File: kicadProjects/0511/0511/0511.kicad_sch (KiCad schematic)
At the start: 28 parts, among them U1 UDA1334A_Breakout, U2 YAAJ_BlackPill, U3 MCP23017, U4 MCP23017, U5 MCP23017, U6 MCP23017, U7 CP2102N-Axx-xQFN24, U8 STM32F411RETx

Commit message: updated backups
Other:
- added sheet Untitled Sheet (untitled.kicad_sch)
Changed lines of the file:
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@@
+	)
+	(sheet
+		(at 260.35 245.11)
+		(size 12.7 3.81)
+		(exclude_from_sim no)
+		(in_bom yes)
+		(on_board yes)
+		(dnp no)
+		(fields_autoplaced yes)
+		(stroke
+			(width 0.1524)
+			(type solid)
+		)
+		(fill
+			(color 0 0 0 0.0000)
+		)
+		(property "Sheetname" "Untitled Sheet"
+			(at 260.35 244.3984 0)
+			(effects
+				(font
+					(size 1.27 1.27)
+				)
+				(justify left bottom)
+			)
+		)
+		(property "Sheetfile" "untitled.kicad_sch"
+			(at 260.35 249.5046 0)
+			(effects
+				(font
+					(size 1.27 1.27)
+				)
+				(justify left top)
+			)
+		)
+		(pin "test" input
+			(at 260.35 247.65 180)
+			(effects
+				(font
+					(size 1.27 1.27)
+				)
+				(justify left)
+			)
+		)
+		(instances
+			(project "0511"
+				(path "/2c0b0e0d-c5e7-48b7-93bb-9be1941509af"
+					(page "69")
+				)
+			)
+		)
 	)
 	(sheet

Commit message: started alim bloc
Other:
- removed sheet Untitled Sheet
- added sheet Buck (buck.kicad_sch)
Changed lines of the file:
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@@
 	(wire
 		(pts
+			(xy 303.53 229.87) (xy 303.53 234.95)
+		)
+		(stroke
+			(width 0)
+			(type default)
+		)
+	)
+	(wire
+		(pts
 			(xy 320.04 50.8) (xy 320.04 53.34)
 		)
@@
 	(wire
 		(pts
+			(xy 266.7 234.95) (xy 266.7 240.03)
+		)
+		(stroke
+			(width 0)
+			(type default)
+		)
+	)
+	(wire
+		(pts
 			(xy 228.6 63.5) (xy 228.6 69.85)
 		)
@@
 	(wire
 		(pts
+			(xy 262.89 240.03) (xy 266.7 240.03)
+		)
+		(stroke
+			(width 0)
+			(type default)
+		)
+	)
+	(wire
+		(pts
 			(xy 156.21 165.1) (xy 156.21 143.51)
 		)
@@
 	(wire
 		(pts
+			(xy 303.53 234.95) (xy 285.75 234.95)
+		)
+		(stroke
+			(width 0)
+			(type default)
+		)
+	)
+	(wire
+		(pts
+			(xy 273.05 234.95) (xy 266.7 234.95)
+		)
+		(stroke
+			(width 0)
+			(type default)
+		)
+	)
+	(wire
+		(pts
 			(xy 331.47 36.83) (xy 331.47 43.18)
 		)
@@
 	)
 	(symbol
+		(lib_id "power:+3.3V")
+		(at 303.53 229.87 0)
+		(unit 1)
+		(exclude_from_sim no)
+		(in_bom yes)
+		(on_board yes)
+		(dnp no)
+		(fields_autoplaced yes)
+		(property "Reference" "#PWR044"
+			(at 303.53 233.68 0)
+			(effects
+				(font
+					(size 1.27 1.27)
+				)
+				(hide yes)
+			)
+		)
+		(property "Value" "+3.3V"
+			(at 303.53 224.79 0)
+			(effects
+				(font
+					(size 1.27 1.27)
+				)
+			)
+		)
+		(property "Footprint" ""
+			(at 303.53 229.87 0)
+			(effects
+				(font
+					(size 1.27 1.27)
+				)
+				(hide yes)
+			)
+		)
+		(property "Datasheet" ""
+			(at 303.53 229.87 0)
+			(effects
+				(font
+					(size 1.27 1.27)
+				)
+				(hide yes)
+			)
+		)
+		(property "Description" "Power symbol creates a global label with name \"+3.3V\""
+			(at 303.53 229.87 0)
+			(effects
+				(font
+					(size 1.27 1.27)
+				)
+				(hide yes)
+			)
+		)
+		(pin "1"
+		)
+		(instances
+			(project "0511"
+				(path "/2c0b0e0d-c5e7-48b7-93bb-9be1941509af"
+					(reference "#PWR044")
+					(unit 1)
+				)
+			)
+		)
+	)
+	(symbol
 		(lib_id "Device:C")
 		(at 34.29 109.22 0)
@@
 	)
 	(symbol
+		(lib_id "power:GND")
+		(at 262.89 240.03 0)
+		(unit 1)
+		(exclude_from_sim no)
+		(in_bom yes)
+		(on_board yes)
+		(dnp no)
+		(fields_autoplaced yes)
+		(property "Reference" "#PWR045"
+			(at 262.89 246.38 0)
+			(effects
+				(font
+					(size 1.27 1.27)
+				)
+				(hide yes)
+			)
+		)
+		(property "Value" "GND"
+			(at 262.89 245.11 0)
+			(effects
+				(font
+					(size 1.27 1.27)
+				)
+			)
+		)
+		(property "Footprint" ""
+			(at 262.89 240.03 0)
+			(effects
+				(font
+					(size 1.27 1.27)
+				)
+				(hide yes)
+			)
+		)
+		(property "Datasheet" ""
+			(at 262.89 240.03 0)
+			(effects
+				(font
+					(size 1.27 1.27)
+				)
+				(hide yes)
+			)
+		)
+		(property "Description" "Power symbol creates a global label with name \"GND\" , ground"
+			(at 262.89 240.03 0)
+			(effects
+				(font
+					(size 1.27 1.27)
+				)
+				(hide yes)
+			)
+		)
+		(pin "1"
+		)
+		(instances
+			(project "0511"
+				(path "/2c0b0e0d-c5e7-48b7-93bb-9be1941509af"
+					(reference "#PWR045")
+					(unit 1)
+				)
+			)
+		)
+	)
+	(symbol
 		(lib_id "power:+3.3V")
 		(at 67.31 86.36 0)
@@
 	)
 	(sheet
+		(at 273.05 232.41)
+		(size 12.7 3.81)
+		(exclude_from_sim no)
+		(in_bom yes)
+		(on_board yes)
+		(dnp no)
+		(fields_autoplaced yes)
+		(stroke
+			(width 0.1524)
+			(type solid)
+		)
+		(fill
+			(color 0 0 0 0.0000)
+		)
+		(property "Sheetname" "Buck"
+			(at 273.05 231.6984 0)
+			(effects
+				(font
+					(size 1.27 1.27)
+				)
+				(justify left bottom)
+			)
+		)
+		(property "Sheetfile" "buck.kicad_sch"
+			(at 273.05 236.8046 0)
+			(effects
+				(font
+					(size 1.27 1.27)
+				)
+				(justify left top)
+			)
+		)
+		(pin "3.3v" input
+			(at 285.75 234.95 0)
+			(effects
+				(font
+					(size 1.27 1.27)
+				)
+				(justify right)
+			)
+		)
+		(pin "gnd" passive
+			(at 273.05 234.95 180)
+			(effects
+				(font
+					(size 1.27 1.27)
+				)
+				(justify left)
+			)
+		)
+		(instances
+			(project "0511"
+				(path "/2c0b0e0d-c5e7-48b7-93bb-9be1941509af"
+					(page "69")
+				)
+			)
+		)
+	)
+	(sheet
 		(at 147.32 167.64)
 		(size 12.7 3.81)
@@
 				)
 			)
-		)
-	)
-	(sheet
-		(at 260.35 245.11)
-		(size 12.7 3.81)
-		(exclude_from_sim no)
-		(in_bom yes)
-		(on_board yes)
-		(dnp no)
-		(fields_autoplaced yes)
-		(stroke
-			(width 0.1524)
-			(type solid)
-		)
-		(fill
-			(color 0 0 0 0.0000)
-		)
-		(property "Sheetname" "Untitled Sheet"
-			(at 260.35 244.3984 0)
-			(effects
-				(font
-					(size 1.27 1.27)
-				)
-				(justify left bottom)
-			)
-		)
-		(property "Sheetfile" "untitled.kicad_sch"
-			(at 260.35 249.5046 0)
-			(effects
-				(font
-					(size 1.27 1.27)
-				)
-				(justify left top)
-			)
-		)
-		(pin "test" input
-			(at 260.35 247.65 180)
-			(effects
-				(font
-					(size 1.27 1.27)
-				)
-				(justify left)
-			)
-		)
-		(instances
-			(project "0511"
-				(path "/2c0b0e0d-c5e7-48b7-93bb-9be1941509af"
-					(page "69")
-				)
-			)

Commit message: started stm32 hierarchical b=view scheme
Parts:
- removed U8: STM32F411RETx, Package_QFP:LQFP-64_10x10mm_P0.5mm, symbol MCU_ST_STM32F4:STM32F411RETx
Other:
- added sheet Stm32f411retx (stm32f411retx.kicad_sch)
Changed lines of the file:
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@@
 	)
 	(symbol
-		(lib_id "MCU_ST_STM32F4:STM32F411RETx")
-		(at 88.9 251.46 90)
-		(unit 1)
-		(exclude_from_sim no)
-		(in_bom yes)
-		(on_board yes)
-		(dnp no)
-		(fields_autoplaced yes)
-		(property "Reference" "U8"
-			(at 140.97 243.4746 90)
-			(effects
-				(font
-					(size 1.27 1.27)
-				)
-			)
-		)
-		(property "Value" "STM32F411RETx"
-			(at 140.97 246.0146 90)
-			(effects
-				(font
-					(size 1.27 1.27)
-				)
-			)
-		)
-		(property "Footprint" "Package_QFP:LQFP-64_10x10mm_P0.5mm"
-			(at 132.08 266.7 0)
-			(effects
-				(font
-					(size 1.27 1.27)
-				)
-				(justify right)
-				(hide yes)
-			)
-		)
-		(property "Datasheet" "https://www.st.com/resource/en/datasheet/stm32f411re.pdf"
-			(at 88.9 251.46 0)
-			(effects
-				(font
-					(size 1.27 1.27)
-				)
-				(hide yes)
-			)
-		)
-		(property "Description" "STMicroelectronics Arm Cortex-M4 MCU, 512KB flash, 128KB RAM, 100 MHz, 1.7-3.6V, 50 GPIO, LQFP64"
-			(at 88.9 251.46 0)
-			(effects
-				(font
-					(size 1.27 1.27)
-				)
-				(hide yes)
-			)
-		)
-		(pin "17"
-		)
-		(pin "52"
-		)
-		(pin "40"
-		)
-		(pin "27"
-		)
-		(pin "59"
-		)
-		(pin "23"
-		)
-		(pin "60"
-		)
-		(pin "54"
-		)
-		(pin "36"
-		)
-		(pin "2"
-		)
-		(pin "26"
-		)
-		(pin "37"
-		)
-		(pin "9"
-		)
-		(pin "41"
-		)
-		(pin "11"
-		)
-		(pin "55"
-		)
-		(pin "20"
-		)
-		(pin "57"
-		)
-		(pin "24"
-		)
-		(pin "16"
-		)
-		(pin "53"
-		)
-		(pin "25"
-		)
-		(pin "31"
-		)
-		(pin "58"
-		)
-		(pin "21"
-		)
-		(pin "18"
-		)
-		(pin "29"
-		)
-		(pin "19"
-		)
-		(pin "63"
-		)
-		(pin "7"
-		)
-		(pin "6"
-		)
-		(pin "5"
-		)
-		(pin "33"
-		)
-		(pin "4"
-		)
-		(pin "62"
-		)
-		(pin "39"
-		)
-		(pin "56"
-		)
-		(pin "35"
-		)
-		(pin "22"
-		)
-		(pin "51"
-		)
-		(pin "42"
-		)
-		(pin "15"
-		)
-		(pin "28"
-		)
-		(pin "64"
-		)
-		(pin "47"
-		)
-		(pin "13"
-		)
-		(pin "38"
-		)
-		(pin "61"
-		)
-		(pin "48"
-		)
-		(pin "12"
-		)
-		(pin "14"
-		)
-		(pin "49"
-		)
-		(pin "45"
-		)
-		(pin "8"
-		)
-		(pin "50"
-		)
-		(pin "43"
-		)
-		(pin "34"
-		)
-		(pin "32"
-		)
-		(pin "44"
-		)
-		(pin "3"
-		)
-		(pin "30"
-		)
-		(pin "1"
-		)
-		(pin "46"
-		)
-		(pin "10"
-		)
-		(instances
-			(project ""
-				(path "/2c0b0e0d-c5e7-48b7-93bb-9be1941509af"
-					(reference "U8")
-					(unit 1)
-				)
-			)
-		)
-	)
-	(symbol
 		(lib_id "power:+3.3V")
 		(at 90.17 71.12 0)
@@
 				)
 			)
+		)
+	)
+	(sheet
+		(at 234.95 220.98)
+		(size 12.7 3.81)
+		(exclude_from_sim no)
+		(in_bom yes)
+		(on_board yes)
+		(dnp no)
+		(fields_autoplaced yes)
+		(stroke
+			(width 0.1524)
+			(type solid)
+		)
+		(fill
+			(color 0 0 0 0.0000)
+		)
+		(property "Sheetname" "Stm32f411retx"
+			(at 234.95 220.2684 0)
+			(effects
+				(font
+					(size 1.27 1.27)
+				)
+				(justify left bottom)
+			)
+		)
+		(property "Sheetfile" "stm32f411retx.kicad_sch"
+			(at 234.95 225.3746 0)
+			(effects
+				(font
+					(size 1.27 1.27)
+				)
+				(justify left top)
+			)
+		)
+		(instances
+			(project "0511"
+				(path "/2c0b0e0d-c5e7-48b7-93bb-9be1941509af"
+					(page "70")
+				)
+			)

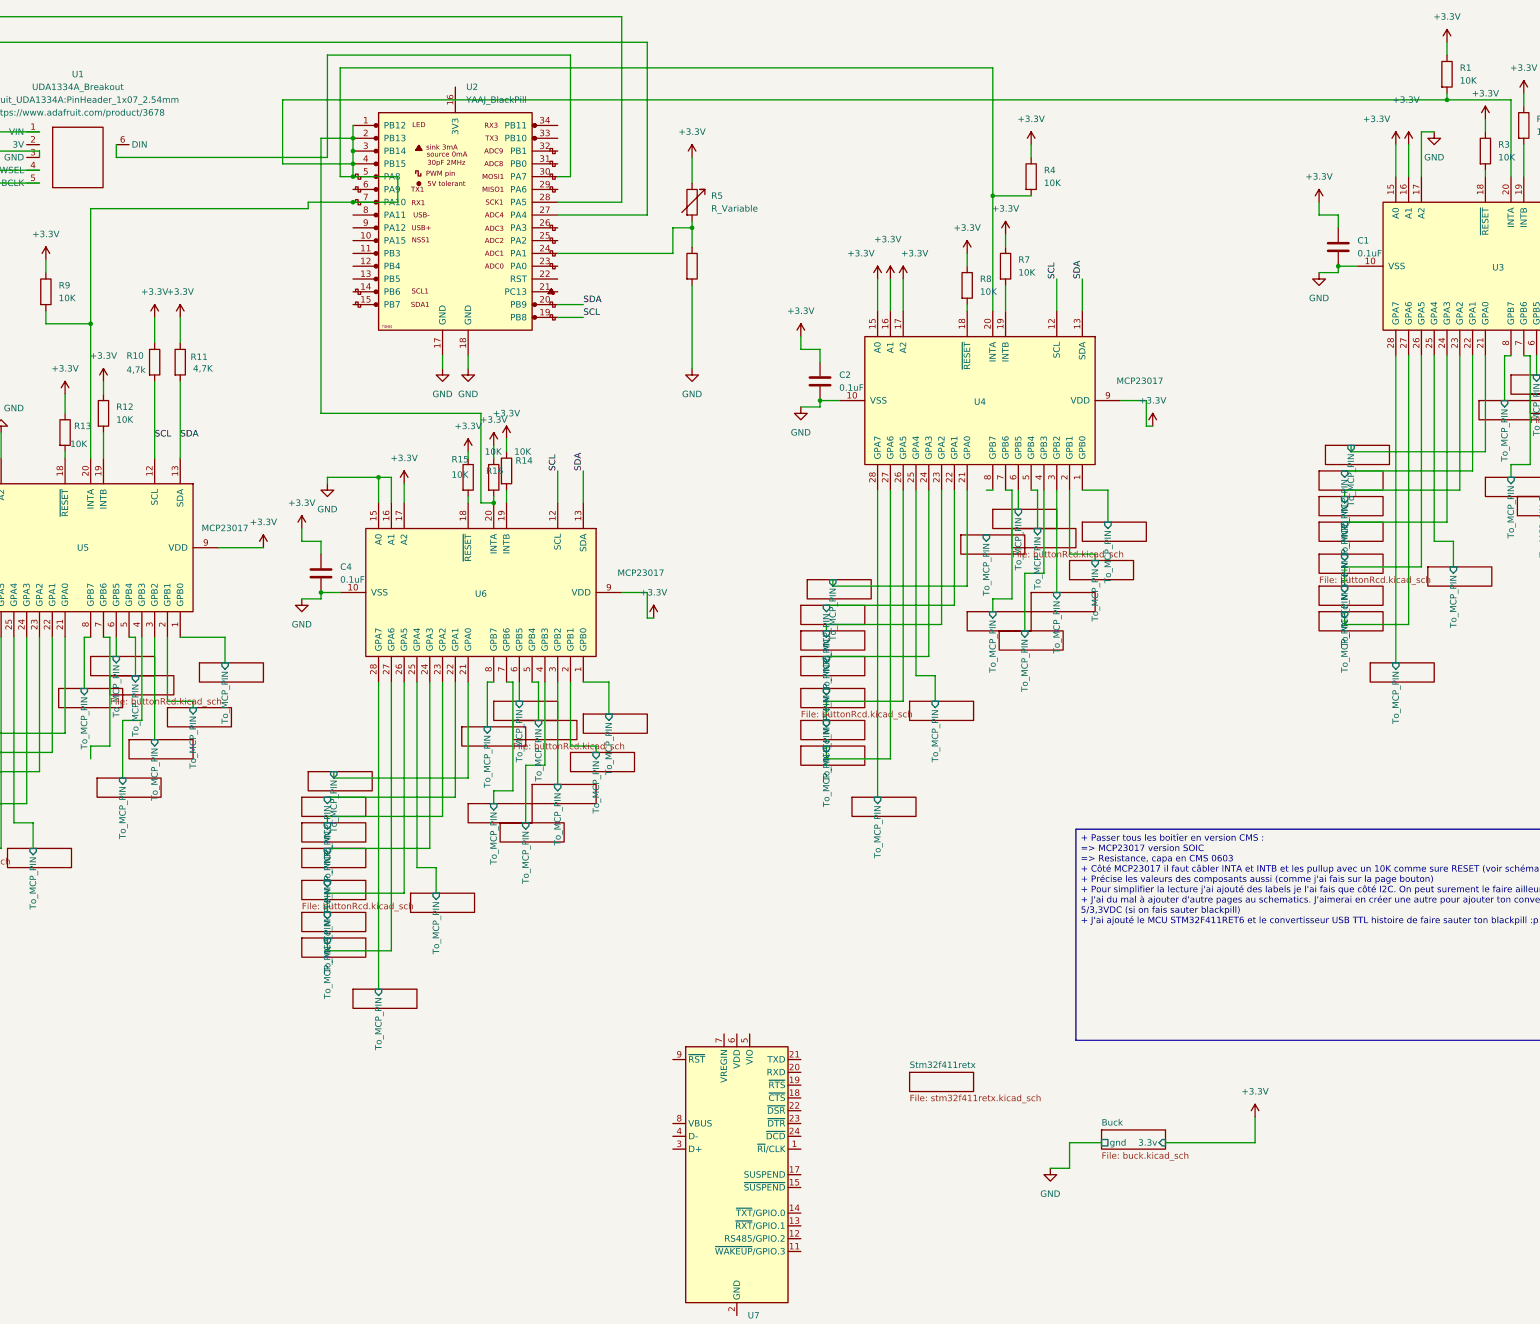
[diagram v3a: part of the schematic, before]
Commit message: started to add hierarchical pins
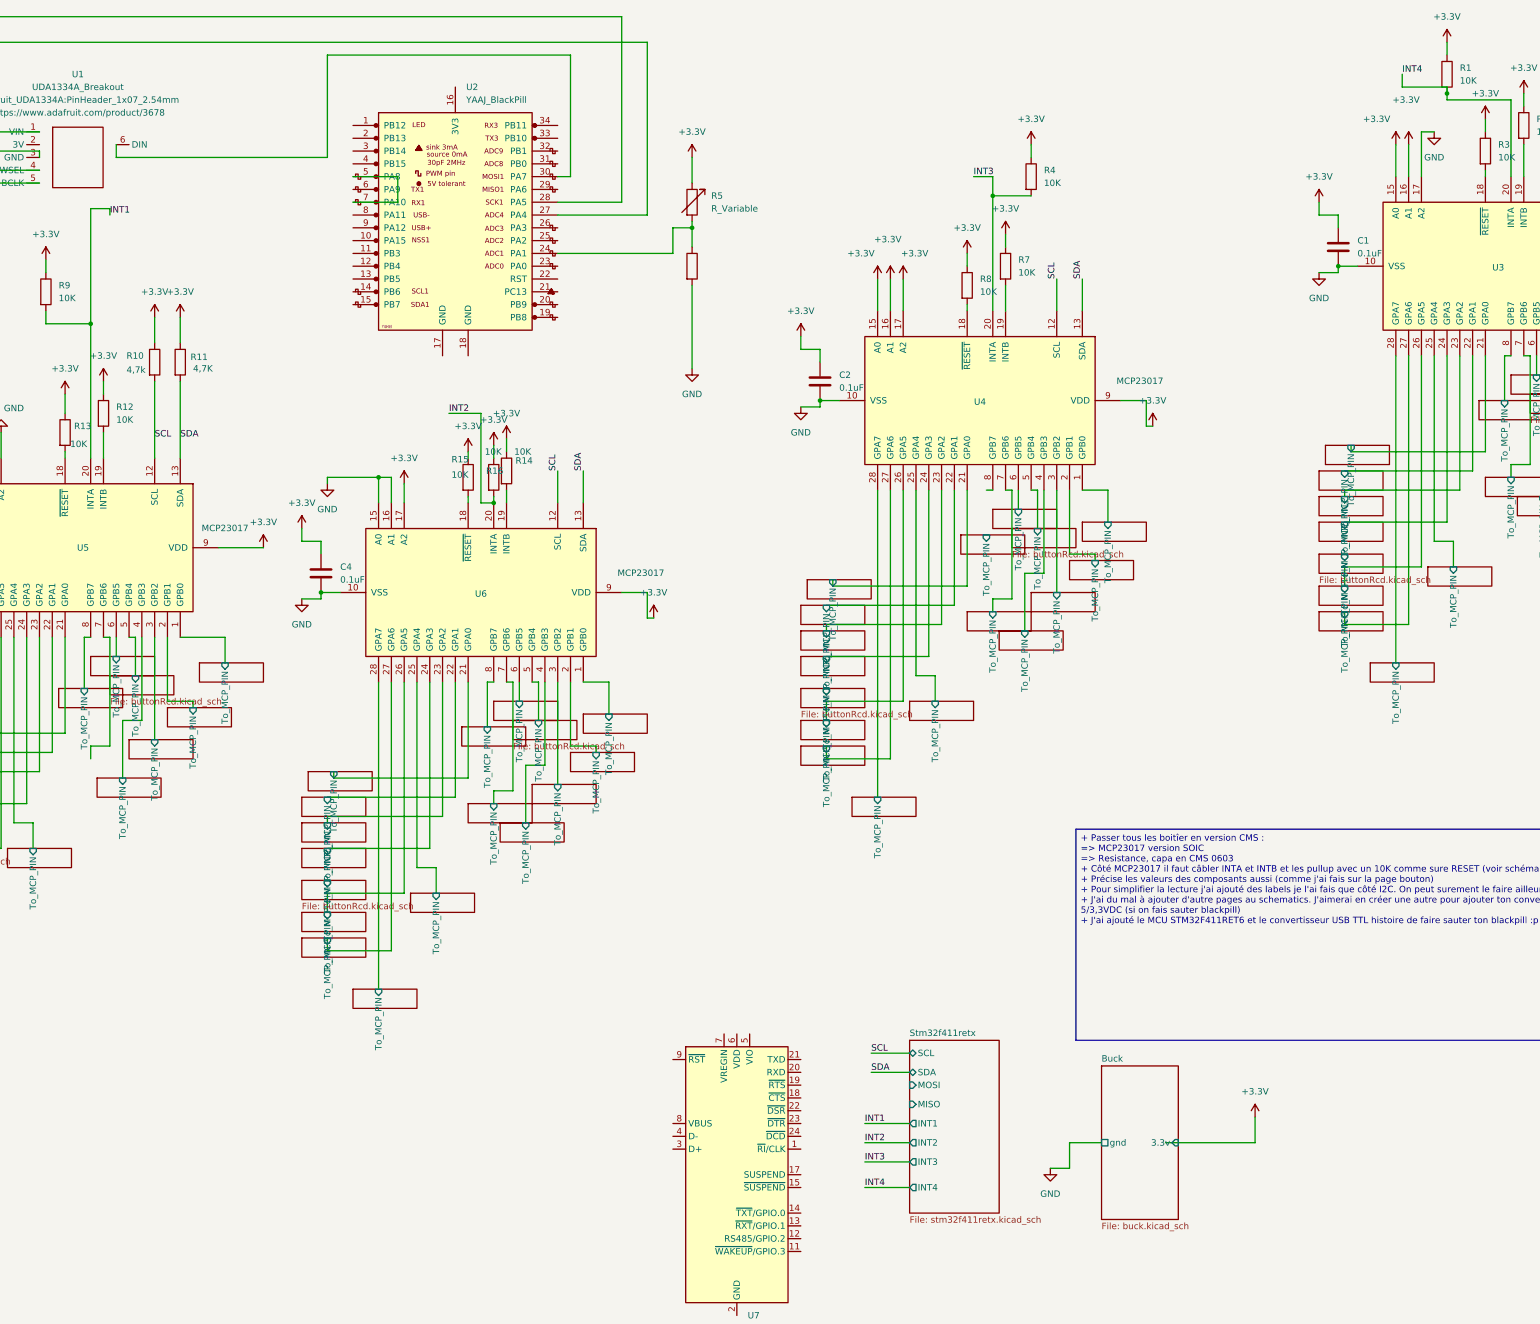
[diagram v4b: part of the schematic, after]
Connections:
- net GND: no longer U2.17 (GND), U2.18 (GND)
- net SCL: no longer U2.19 (PB8)
- net SDA: no longer U2.20 (PB9)
- new net: U2.5 (PA8), U2.7 (PA10)
- new net INT1: R9.2, U5.20 (INTA)
- new net INT2: R16.2, U6.20 (INTA)
- new net INT3: R4.2, U4.20 (INTA)
- new net INT4: R1.2, U3.20 (INTA)
- now unconnected: U2.1 (PB12), U2.2 (PB13), U2.3 (PB14), U2.4 (PB15)
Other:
- sheet Stm32f411retx ports: added INT1, INT2, INT3, INT4, MISO, MOSI, SCL, SDA; removed none
